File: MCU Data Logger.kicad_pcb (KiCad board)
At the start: 2 copper layers, 46.4 x 36.6 mm, 29 parts, among them J1 Conn_01x04_Pin, J2 Conn_01x04_Pin, J3 Conn_01x09_Pin, J4 Conn_02x03_Odd_Even, U1 24LC1025, U2 24LC1025, U3 ATmega328P, U4 DS1337S_, Y1 16MHz, Y2 32.768 KHz

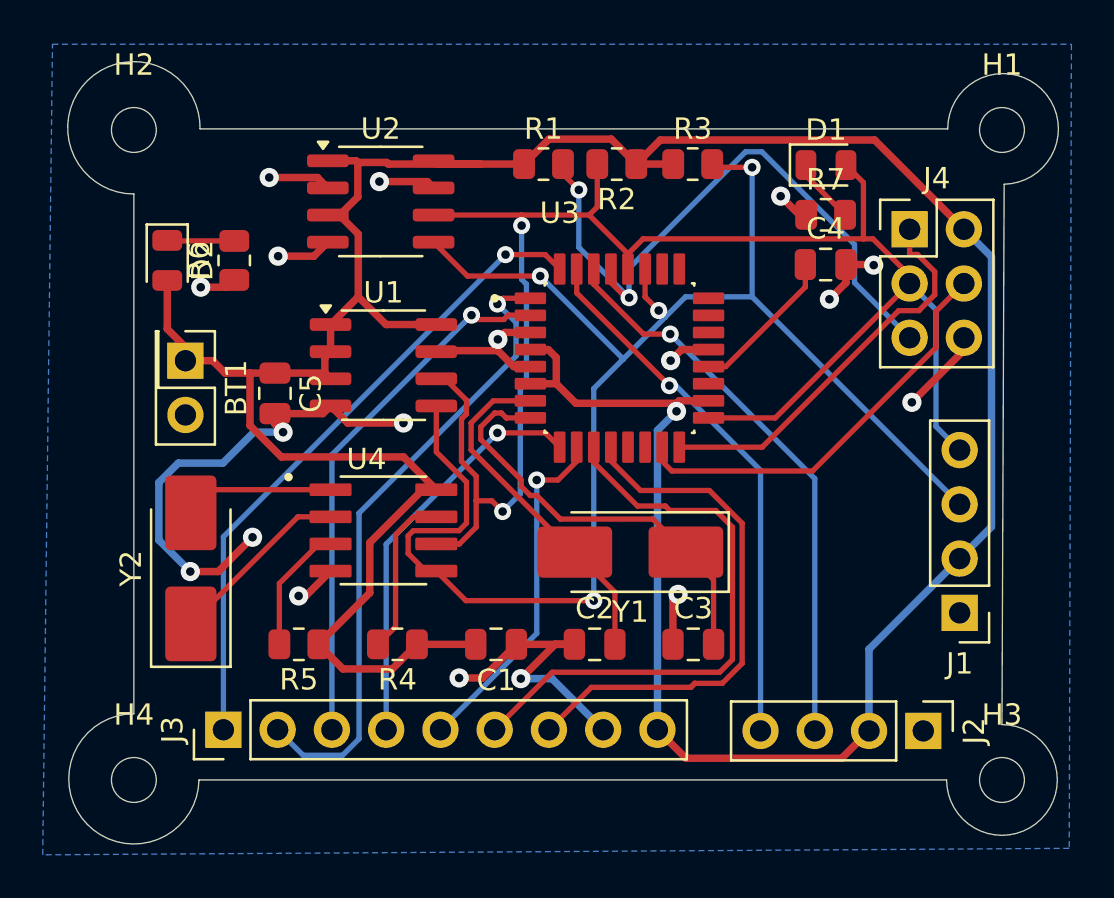
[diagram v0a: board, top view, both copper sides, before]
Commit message: Finishing the 2Layer Version
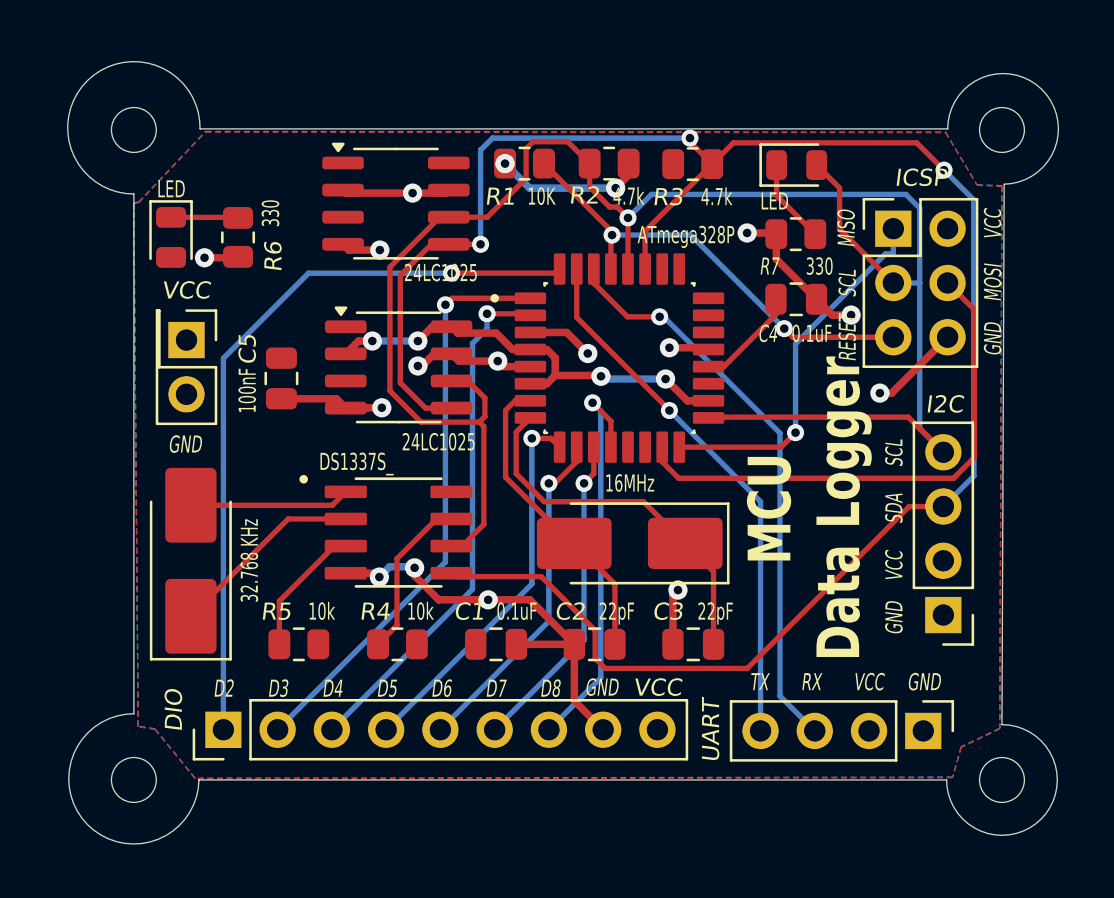
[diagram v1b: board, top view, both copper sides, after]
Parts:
- moved C4 2.13 mm to (158.0, 41.0)
- moved R7 1.67 mm to (158.0, 37.9)
- moved D1 1.37 mm to (158.0, 34.7)
- moved D2 1.09 mm to (128.7, 38.1)
- moved R6 1.09 mm to (131.9, 38.1)
- moved VCC 0.97 mm to (129.5, 42.9)
- moved R1 0.89 mm to (145.3, 34.6)
- moved I2C 0.77 mm to (164.9, 55.8)
- moved ICSP 0.76 mm to (162.6, 37.7)
- moved C5 0.76 mm to (133.9, 44.7)
- moved U2 0.72 mm to (139.3, 36.5)
- moved U1 0.72 mm to (139.4, 44.2)
- moved U4 0.72 mm to (139.4, 51.9)
- moved Y1 0.41 mm to (150.2, 52.4)
- moved R2 0.36 mm to (149.3, 34.6)
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- renumbered J3 to DIO, J1 to I2C, J4 to ICSP, J2 to UART, BT1 to VCC
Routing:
- net /VCC: track 159.7 -> 27.8 mm, vias 1 -> 6
- net /SDA: track 74.1 -> 92.1 mm, vias 4 -> 3
- net /D7: track 27.1 -> 15.2 mm, vias 0 -> 1
- net GND: track 68.8 -> 58.1 mm, vias 18 -> 15
- net /RESET: track 30.7 -> 21.4 mm
- net /SCL: track 78.5 -> 85.6 mm, vias 2 -> 1
- net /D8: track 25.2 -> 18.9 mm, vias 0 -> 1
- net /MOSI: track 19.6 -> 24.7 mm
- net /D2: track 30.5 -> 34.9 mm
- net /D3: track 30.0 -> 27.3 mm
- net Net-(U3-XTAL2/PB7): track 20.1 -> 17.4 mm
- net Net-(U3-AREF): track 7.13 -> 4.88 mm
- net Net-(U3-XTAL1/PB6): track 16.4 -> 14.5 mm
- net /D5: track 19.2 -> 17.9 mm
- net /MISO: track 18.7 -> 17.4 mm, vias 0 -> 1
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- added copper zone on F.Cu, net /VCC
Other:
- board text added: "D2"
- board text added: "D3"
- board text added: "D4"
- board text added: "D5"
- board text added: "D6"
- board text added: "D7"
- board text added: "D8"
- board text added: "Data Logger With ATMega328P - 2MB EEPROM - RTC - I2C, SPI, GPIO"
- board text added: "Designed By: Eng. Zeyad Hisham"
- board text added: "GND"
- board text added: "MCU Data Logger"
- board text added: "MISO"
- board text added: "MOSI"
- board text added: "RESET"
- board text added: "RX"
- board text added: "SCL"
- board text added: "SDA"
- board text added: "TX"
- board text added: "VCC"

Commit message: Completed 2layer board design
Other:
- board text added: "0.2000 mm / 0.0000 mm"
- board text added: "0.3000 mm"
- board text added: "1.6000 mm"
- board text added: "2"
- board text added: "46.3814 mm x 36.6290 mm"
- board text added: "BOARD CHARACTERISTICS"
- board text added: "Board Thickness:"
- board text added: "Board overall dimensions:"
- board text added: "Castellated pads:"
- board text added: "Copper Finish:"
- board text added: "Copper Layer Count:"
- board text added: "Edge card connectors:"
- board text added: "Impedance Control:"
- board text added: "Min hole diameter:"
- board text added: "Min track/spacing:"
- board text added: "No"
- board text added: "None"
- board text added: "Plated Board Edge:"
